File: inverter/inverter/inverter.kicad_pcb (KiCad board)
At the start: 2 copper layers, 13 x 10 mm, 6 parts, among them J1 in, J2 VDD, J3 VSS, J4 out, P1 P

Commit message: Created buffer and updated file organisation
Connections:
- net Net-(J1-Pad1) renamed /Inv_1/in
- net Net-(J2-Pad1) renamed VDD
- net Net-(J3-Pad1) renamed VSS
- net Net-(J4-Pad1) renamed /Inv_1/out
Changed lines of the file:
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@@
   )
   (net 0 "")
-  (net 1 "Net-(J1-Pad1)")
-  (net 2 "Net-(J2-Pad1)")
-  (net 3 "Net-(J3-Pad1)")
-  (net 4 "Net-(J4-Pad1)")
+  (net 1 /Inv_1/in)
+  (net 2 VDD)
+  (net 3 VSS)
+  (net 4 /Inv_1/out)
   (net_class Default "This is the default net class."
     (clearance 0.2)
@@
     (uvia_dia 0.3)
     (uvia_drill 0.1)
-    (add_net "Net-(J1-Pad1)")
-    (add_net "Net-(J2-Pad1)")
-    (add_net "Net-(J3-Pad1)")
-    (add_net "Net-(J4-Pad1)")
+    (add_net /Inv_1/in)
+    (add_net /Inv_1/out)
+    (add_net VDD)
+    (add_net VSS)
   )
   (module Wire_Pads:SolderWirePad_single_SMD_5x10mm (layer F.Cu)
@@
     (fp_line (start -2.75 -5.25) (end -2.75 5.25) (layer F.CrtYd) (width 0.05))
     (pad 1 smd rect (at 0 0 90) (size 5 2.5) (layers F.Cu F.Paste F.Mask)
-      (net 1 "Net-(J1-Pad1)"))
+      (net 1 /Inv_1/in))
   )
   (module Wire_Pads:SolderWirePad_single_SMD_5x10mm (layer F.Cu)
@@
     (fp_line (start 2.75 -5.25) (end -2.75 -5.25) (layer F.CrtYd) (width 0.05))
     (pad 1 smd rect (at 0 0) (size 5 2.5) (layers F.Cu F.Paste F.Mask)
-      (net 2 "Net-(J2-Pad1)"))
+      (net 2 VDD))
   )
   (module Wire_Pads:SolderWirePad_single_SMD_5x10mm (layer F.Cu)
@@
     (fp_line (start 2.75 -5.25) (end -2.75 -5.25) (layer F.CrtYd) (width 0.05))
     (pad 1 smd rect (at 0 0) (size 5 2.5) (layers F.Cu F.Paste F.Mask)
-      (net 3 "Net-(J3-Pad1)"))
+      (net 3 VSS))
   )
   (module Wire_Pads:SolderWirePad_single_SMD_5x10mm (layer F.Cu)
@@
     (fp_line (start -2.75 -5.25) (end -2.75 5.25) (layer F.CrtYd) (width 0.05))
     (pad 1 smd rect (at 0 0 90) (size 5 2.5) (layers F.Cu F.Paste F.Mask)
-      (net 4 "Net-(J4-Pad1)"))
+      (net 4 /Inv_1/out))
   )
   (module TO_SOT_Packages_SMD:TSOT-23 (layer F.Cu)
@@
     )
     (pad 3 smd rect (at 1.31 0) (size 1.22 0.65) (layers F.Cu F.Paste F.Mask)
-      (net 4 "Net-(J4-Pad1)"))
+      (net 4 /Inv_1/out))
     (pad 2 smd rect (at -1.31 0.95) (size 1.22 0.65) (layers F.Cu F.Paste F.Mask)
-      (net 3 "Net-(J3-Pad1)"))
+      (net 3 VSS))
     (pad 1 smd rect (at -1.31 -0.95) (size 1.22 0.65) (layers F.Cu F.Paste F.Mask)
-      (net 1 "Net-(J1-Pad1)"))
+      (net 1 /Inv_1/in))
     (model ${KISYS3DMOD}/TO_SOT_Packages_SMD.3dshapes/TSOT-23.wrl
       (at (xyz 0 0 0))
@@
     (fp_line (start 2.17 -1.7) (end -2.17 -1.7) (layer B.CrtYd) (width 0.05))
     (pad 1 smd rect (at -1.31 0.95) (size 1.22 0.65) (layers B.Cu B.Paste B.Mask)
-      (net 1 "Net-(J1-Pad1)"))
+      (net 1 /Inv_1/in))
     (pad 2 smd rect (at -1.31 -0.95) (size 1.22 0.65) (layers B.Cu B.Paste B.Mask)
-      (net 4 "Net-(J4-Pad1)"))
+      (net 4 /Inv_1/out))
     (pad 3 smd rect (at 1.31 0) (size 1.22 0.65) (layers B.Cu B.Paste B.Mask)
-      (net 2 "Net-(J2-Pad1)"))
+      (net 2 VDD))
     (model ${KISYS3DMOD}/TO_SOT_Packages_SMD.3dshapes/TSOT-23.wrl
       (at (xyz 0 0 0))

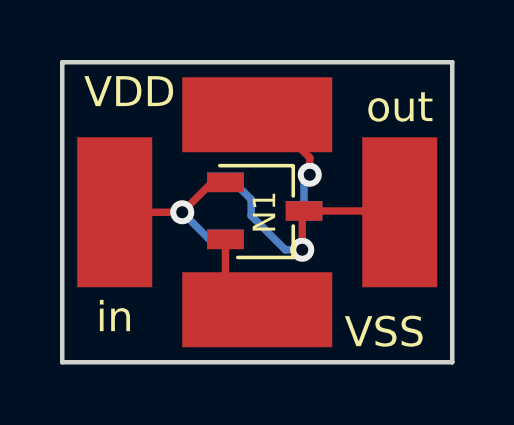
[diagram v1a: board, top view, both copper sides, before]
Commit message: Fixed a broken circuit
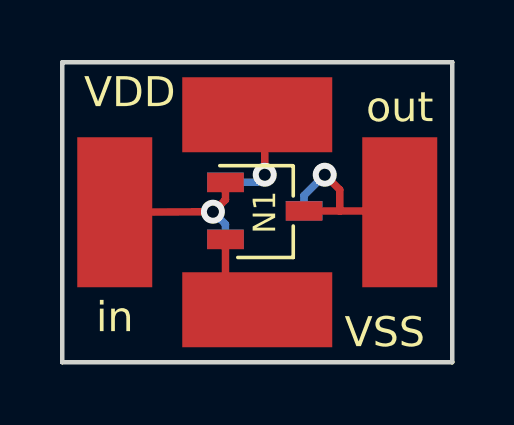
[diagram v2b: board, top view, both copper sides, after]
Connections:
- P1 pad 2: /Inv_1/out -> VDD
- P1 pad 3: VDD -> /Inv_1/out
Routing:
- net /Inv_1/out: track 8.64 -> 6.11 mm
- net VDD: track 4.19 -> 3.52 mm
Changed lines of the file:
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@@
     (thickness 1.6)
     (drawings 5)
-    (tracks 25)
+    (tracks 23)
     (zones 0)
     (modules 6)
@@
       (net 1 /Inv_1/in))
     (pad 2 smd rect (at -1.31 -0.95) (size 1.22 0.65) (layers B.Cu B.Paste B.Mask)
+      (net 2 VDD))
+    (pad 3 smd rect (at 1.31 0) (size 1.22 0.65) (layers B.Cu B.Paste B.Mask)
       (net 4 /Inv_1/out))
-    (pad 3 smd rect (at 1.31 0) (size 1.22 0.65) (layers B.Cu B.Paste B.Mask)
-      (net 2 VDD))
     (model ${KISYS3DMOD}/TO_SOT_Packages_SMD.3dshapes/TSOT-23.wrl
       (at (xyz 0 0 0))
@@
   (gr_line (start 168.25 89.25) (end 181.25 89.25) (layer Edge.Cuts) (width 0.15))
   (gr_line (start 168.25 79.25) (end 168.25 89.25) (layer Edge.Cuts) (width 0.15))
-  (segment (start 172.25 84.25) (end 170 84.25) (width 0.25) (layer F.Cu) (net 1))
-  (segment (start 173.69 85.15) (end 173.15 85.15) (width 0.25) (layer B.Cu) (net 1))
-  (segment (start 173.15 85.15) (end 172.25 84.25) (width 0.25) (layer B.Cu) (net 1))
-  (segment (start 173.69 83.2575) (end 173.2425 83.2575) (width 0.25) (layer F.Cu) (net 1))
-  (segment (start 173.2425 83.2575) (end 172.25 84.25) (width 0.25) (layer F.Cu) (net 1))
-  (via (at 172.25 84.25) (size 0.8) (drill 0.4) (layers F.Cu B.Cu) (net 1))
-  (segment (start 176.5 83) (end 176.5 82.434315) (width 0.25) (layer F.Cu) (net 2))
-  (segment (start 176.5 82.434315) (end 175.065685 81) (width 0.25) (layer F.Cu) (net 2))
-  (segment (start 175.065685 81) (end 174.75 81) (width 0.25) (layer F.Cu) (net 2))
-  (segment (start 176.31 84.2) (end 176.31 83.19) (width 0.25) (layer B.Cu) (net 2))
-  (segment (start 176.31 83.19) (end 176.5 83) (width 0.25) (layer B.Cu) (net 2))
-  (via (at 176.5 83) (size 0.8) (drill 0.4) (layers F.Cu B.Cu) (net 2))
-  (segment (start 173.69 85.1575) (end 173.69 86.44) (width 0.25) (layer F.Cu) (net 3))
-  (segment (start 173.69 86.44) (end 174.75 87.5) (width 0.25) (layer F.Cu) (net 3))
-  (segment (start 176.25 85.5) (end 176.25 84.2675) (width 0.25) (layer F.Cu) (net 4))
-  (segment (start 176.25 84.2675) (end 176.31 84.2075) (width 0.25) (layer F.Cu) (net 4))
-  (segment (start 175.684315 85.5) (end 176.25 85.5) (width 0.25) (layer B.Cu) (net 4))
-  (segment (start 173.975 83.25) (end 174.55 83.825) (width 0.25) (layer B.Cu) (net 4))
-  (segment (start 174.55 83.825) (end 174.55 84.365685) (width 0.25) (layer B.Cu) (net 4))
-  (segment (start 175.94 85.5) (end 176.25 85.5) (width 0.25) (layer B.Cu) (net 4))
-  (segment (start 173.69 83.25) (end 173.975 83.25) (width 0.25) (layer B.Cu) (net 4))
-  (segment (start 174.55 84.365685) (end 175.684315 85.5) (width 0.25) (layer B.Cu) (net 4))
-  (via (at 176.25 85.5) (size 0.8) (drill 0.4) (layers F.Cu B.Cu) (net 4))
-  (segment (start 176.31 84.2075) (end 179.4575 84.2075) (width 0.25) (layer F.Cu) (net 4))
+  (segment (start 173.69 85.15) (end 173.69 84.649998) (width 0.25) (layer B.Cu) (net 1))
+  (segment (start 173.69 84.649998) (end 173.2725 84.232498) (width 0.25) (layer B.Cu) (net 1))
+  (segment (start 173.5225 84) (end 173.69 83.8325) (width 0.25) (layer F.Cu) (net 1))
+  (segment (start 170 84.25) (end 173.2725 84.232498) (width 0.25) (layer F.Cu) (net 1))
+  (segment (start 173.5225 84) (end 173.504998 84) (width 0.25) (layer F.Cu) (net 1))
+  (segment (start 173.504998 84) (end 173.2725 84.232498) (width 0.25) (layer F.Cu) (net 1))
+  (via (at 173.2725 84.232498) (size 0.8) (drill 0.4) (layers F.Cu B.Cu) (net 1))
+  (segment (start 173.69 83.8325) (end 173.69 83.2575) (width 0.25) (layer F.Cu) (net 1))
+  (segment (start 175 83) (end 175 81.25) (width 0.25) (layer F.Cu) (net 2))
+  (segment (start 175 81.25) (end 174.75 81) (width 0.25) (layer F.Cu) (net 2))
+  (segment (start 173.69 83.25) (end 174.75 83.25) (width 0.25) (layer B.Cu) (net 2))
+  (segment (start 174.75 83.25) (end 175 83) (width 0.25) (layer B.Cu) (net 2))
+  (via (at 175 83) (size 0.8) (drill 0.4) (layers F.Cu B.Cu) (net 2))
+  (segment (start 173.69 85.1575) (end 173.69 86.44) (width 0.25) (layer F.Cu) (net 3) (status 30))
+  (segment (start 173.69 86.44) (end 174.75 87.5) (width 0.25) (layer F.Cu) (net 3) (status 30))
+  (segment (start 176.31 84.2075) (end 177.5 84.2075) (width 0.25) (layer F.Cu) (net 4))
+  (segment (start 177 83) (end 177.5 83.5) (width 0.25) (layer F.Cu) (net 4))
+  (segment (start 177.5 84.2075) (end 179.4575 84.2075) (width 0.25) (layer F.Cu) (net 4))
+  (segment (start 177.5 83.5) (end 177.5 84.2075) (width 0.25) (layer F.Cu) (net 4))
+  (segment (start 176.31 84.2) (end 176.31 83.69) (width 0.25) (layer B.Cu) (net 4))
+  (segment (start 176.31 83.69) (end 177 83) (width 0.25) (layer B.Cu) (net 4))
+  (via (at 177 83) (size 0.8) (drill 0.4) (layers F.Cu B.Cu) (net 4))
   (segment (start 179.4575 84.2075) (end 179.5 84.25) (width 0.25) (layer F.Cu) (net 4))
 )
